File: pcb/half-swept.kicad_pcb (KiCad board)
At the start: 2 copper layers, 108.6 x 88.8 mm, 61 parts, among them J1 AudioJack4dpb, J2 AudioJack4dpb, SW1 SW_Push, SW10 SW_Push, SW11 SW_Push, SW12 SW_Push, SW14 SW_Push, SW15 SW_Push, SW16 SW_Push, SW17 SW_Push, SW18 SW_Push, SW2 SW_Push, SW20 SW_Push, SW21 SW_Push, SW3 SW_Push, SW4 SW_Push, SW5 SW_Push, SW6 SW_Push, SW8 SW_Push, SW9 SW_Push, U2 Elite-C

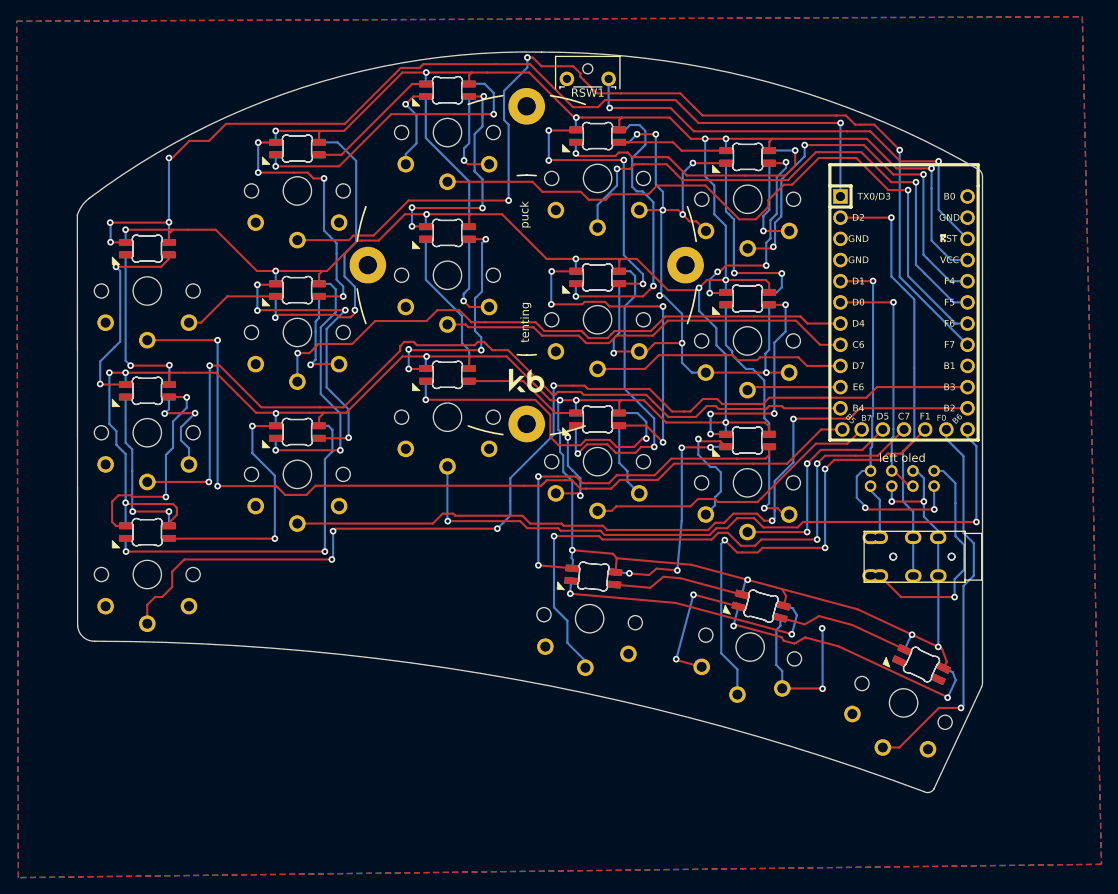
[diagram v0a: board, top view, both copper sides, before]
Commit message: made switch hole sizes a bit bigger to support mill max sockets
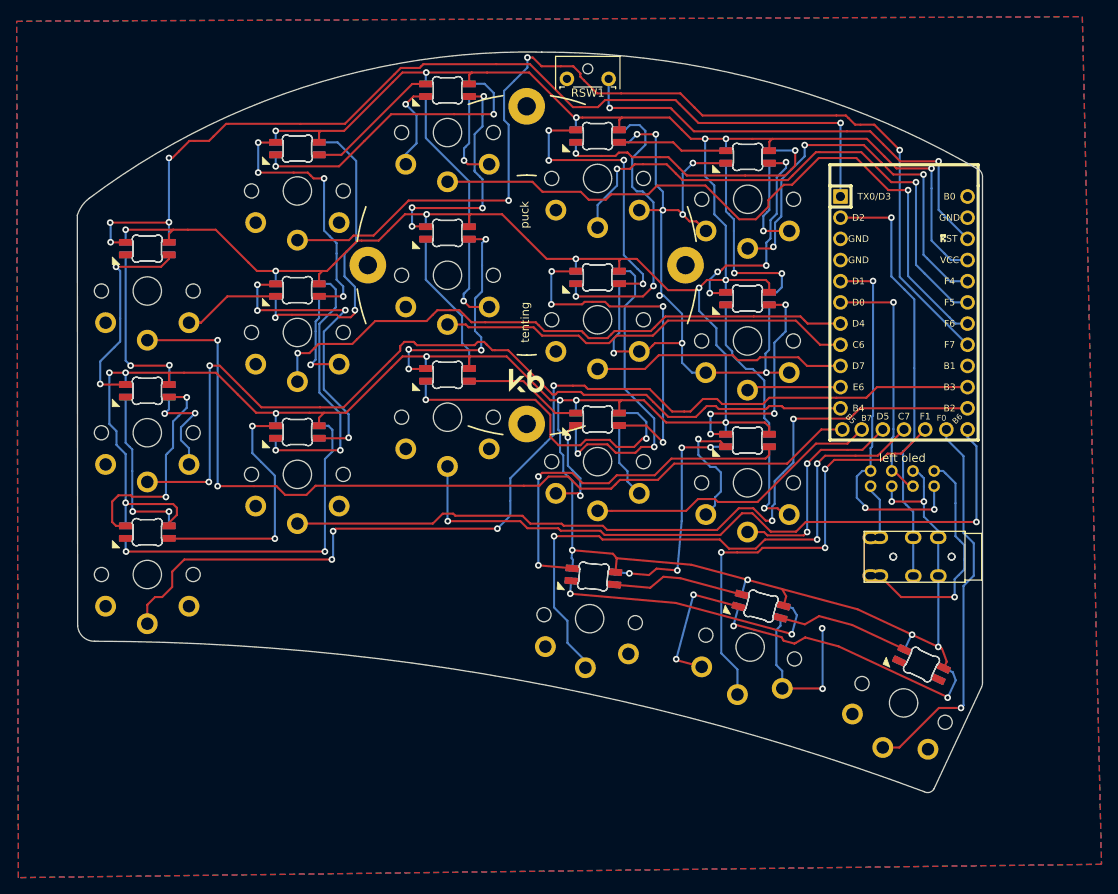
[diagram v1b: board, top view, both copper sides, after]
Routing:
- net Switch17: track 56.0 -> 54.0 mm
- net Switch13: track 83.8 -> 84.7 mm
- net Switch12: track 94.1 -> 94.6 mm
